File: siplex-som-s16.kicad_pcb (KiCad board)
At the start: 6 copper layers, 30 x 30 mm, 47 parts, among them J1 RFShield_OnePiece, J2 Conn_01x20, J3 Conn_01x20, J4 Conn_01x20, J6 Conn_01x20, U1 STM32H743IIKx, U2 IS42S16160J-6BLI, U3 W25Q32JVZP, Y1 25MHz, Y2 32.768KHz

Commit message: Add power
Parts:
- added C34: 2u2, Capacitor_SMD:C_0402_1005Metric, F.Cu at (133.7, 106.0)
- added C35: 100n, Capacitor_SMD:C_0201_0603Metric, F.Cu at (132.7, 106.0)
- added C36: 1u, Capacitor_SMD:C_0402_1005Metric, F.Cu at (130.5, 109.4)
- added C37: 100n, Capacitor_SMD:C_0201_0603Metric, F.Cu at (130.5, 108.5)
- added C38: 1u, Capacitor_SMD:C_0402_1005Metric, F.Cu at (129.1, 92.1)
- added C39: 100n, Capacitor_SMD:C_0201_0603Metric, F.Cu at (129.1, 91.2)
- added L1: L_Small, Inductor_SMD:L_0402_1005Metric, F.Cu at (129.1, 93.2)
- added U4: AP2112K-3.3, Package_TO_SOT_SMD:SOT-23-5, F.Cu at (130.5, 106.0)
- moved C8 18.7 mm to (129.0, 89.3), turned to 90 degrees
- moved R2 18.0 mm to (133.6, 89.1), turned to -90 degrees
- moved C2 17.2 mm to (130.3, 88.8), turned to 90 degrees
- moved R3 11.6 mm to (142.1, 94.4), turned to 90 degrees
- moved C3 6.28 mm to (134.4, 89.1), turned to -90 degrees
- moved C1 5.60 mm to (129.1, 98.6)
- moved C10 4.27 mm to (132.8, 87.5), turned to -90 degrees
- moved C15 1.74 mm to (132.0, 87.5), turned to -90 degrees
- moved C6 1.67 mm to (139.7, 89.3), turned to 0 degrees
- moved R1 1.62 mm to (142.1, 91.4)
- moved C11 1.57 mm to (129.1, 97.3)
- moved C12 1.57 mm to (129.1, 95.6)
- moved C13 1.57 mm to (129.1, 96.4)
- moved C14 1.57 mm to (142.1, 92.9)
- moved C16 1.57 mm to (131.1, 89.0)
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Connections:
- C10 pad 2: +3V3 -> VDD_MCU
- C11 pad 2: +3V3 -> VDD_MCU
- C12 pad 2: +3V3 -> VDD_MCU
- C13 pad 2: +3V3 -> VDD_MCU
- C14 pad 2: +3V3 -> VDD_MCU
- C15 pad 2: +3V3 -> VDD_MCU
- C16 pad 2: +3V3 -> VDD_MCU
- C17 pad 2: +3V3 -> VDD_MCU
- C18 pad 2: +3V3 -> VDD_MCU
- C19 pad 2: +3V3 -> VDD_MCU
- C20 pad 2: +3V3 -> VDD_MCU
- C21 pad 2: +3V3 -> VDD_MCU
- C22 pad 2: +3V3 -> VDD_MCU
- C23 pad 2: +3V3 -> VDD_MCU
- C24 pad 2: +3V3 -> VDD_MCU
- C25 pad 2: +3V3 -> VDD_MCU
- C8 pad 1: +3V3 -> VDDA
- C9 pad 2: +3V3 -> VDDA
- R1 pad 1: +3V3 -> VDD_MCU
- R2 pad 1: +3V3 -> VDD_MCU
- U1 pad A3: unconnected-(U1-PE1-PadA3) -> /MCU/SDRAM_DQMH
- U1 pad A4: unconnected-(U1-PE0-PadA4) -> /MCU/SDRAM_DQML
- U1 pad B15: unconnected-(U1-PA12-PadB15) -> /MCU/USB_DP
- U1 pad B6: unconnected-(U1-PB6-PadB6) -> /MEMORY_FLASH/~{CS}
- U1 pad B7: unconnected-(U1-PG15-PadB7) -> /MCU/~{SDRAM_CAS}
- U1 pad C15: unconnected-(U1-PA11-PadC15) -> /MCU/USB_DN
- U1 pad C5: +3V3 -> VDD_MCU
- U1 pad C7: +3V3 -> VDD_MCU
- U1 pad C8: +3V3 -> VDD_MCU
- U1 pad C9: +3V3 -> VDD_MCU
- U1 pad E15: unconnected-(U1-PA9-PadE15) -> /MCU/USB_VBUS_DET
- U1 pad E2: unconnected-(U1-PF0-PadE2) -> /MCU/SDRAM_A0
- U1 pad F3: +3V3 -> VDD_MCU
- U1 pad F4: unconnected-(U1-PH2-PadF4) -> /MCU/SDRAM_CKE
- U1 pad G13: +3V3 -> VDD_MCU
- U1 pad G3: +3V3 -> VDD_MCU
- U1 pad H13: +3V3 -> VDD_MCU
- U1 pad H14: unconnected-(U1-PG8-PadH14) -> /MCU/SDRAM_CLK
- U1 pad H2: unconnected-(U1-PF2-PadH2) -> /MCU/SDRAM_A2
- U1 pad H3: unconnected-(U1-PF1-PadH3) -> /MCU/SDRAM_A1
- U1 pad J12: +3V3 -> VDD_MCU
- U1 pad J13: +3V3 -> VDD_MCU
- U1 pad J2: unconnected-(U1-PF3-PadJ2) -> /MCU/SDRAM_A3
- U1 pad J3: unconnected-(U1-PF4-PadJ3) -> /MCU/SDRAM_A4
- U1 pad J4: unconnected-(U1-PH5-PadJ4) -> /MCU/~{SDRAM_WE}
- U1 pad K1: unconnected-(U1-PF7-PadK1) -> /MEMORY_FLASH/IO2
- U1 pad K13: unconnected-(U1-PG5-PadK13) -> /MCU/SDRAM_BA1
- U1 pad K14: unconnected-(U1-PG4-PadK14) -> /MCU/SDRAM_BA0
- U1 pad K2: unconnected-(U1-PF6-PadK2) -> /MEMORY_FLASH/IO3
- U1 pad K3: unconnected-(U1-PF5-PadK3) -> /MCU/SDRAM_A5
- U1 pad K4: +3V3 -> VDD_MCU
- U1 pad L15: unconnected-(U1-PG2-PadL15) -> /MCU/SDRAM_A12
- U1 pad L2: unconnected-(U1-PF9-PadL2) -> /MEMORY_FLASH/DI(IO0)
- U1 pad L3: unconnected-(U1-PF8-PadL3) -> /MEMORY_FLASH/DO(IO1)
- U1 pad M4: unconnected-(U1-PC2_C-PadM4) -> /MCU/~{SDRAM_CS}
- U1 pad M6: unconnected-(U1-PB2-PadM6) -> /MEMORY_FLASH/CLK
- U1 pad M7: unconnected-(U1-PG1-PadM7) -> /MCU/SDRAM_A11
- U1 pad N10: +3V3 -> VDD_MCU
- U1 pad N6: unconnected-(U1-PF13-PadN6) -> /MCU/SDRAM_A7
- U1 pad N7: unconnected-(U1-PG0-PadN7) -> /MCU/SDRAM_A10
- U1 pad N8: +3V3 -> VDD_MCU
- U1 pad N9: +3V3 -> VDD_MCU
- U1 pad P1: +3V3 -> VDDA
- U1 pad P6: unconnected-(U1-PF12-PadP6) -> /MCU/SDRAM_A6
- U1 pad P7: unconnected-(U1-PF15-PadP7) -> /MCU/SDRAM_A9
- U1 pad R1: +3V3 -> VDDA
- U1 pad R6: unconnected-(U1-PF11-PadR6) -> /MCU/~{SDRAM_RAS}
- U1 pad R7: unconnected-(U1-PF14-PadR7) -> /MCU/SDRAM_A8
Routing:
- net GND: track 0.00 -> 21.9 mm, vias 0 -> 46
- net +3V3: track 24.7 -> 3.96 mm, vias 0 -> 7
- net VDD_MCU: track 0.00 -> 6.43 mm, vias 0 -> 14
- net Net-(U1-PC15): track 5.79 -> 0.46 mm, vias 0 -> 1
- net Net-(U1-PC14): track 5.09 -> 0.46 mm, vias 0 -> 1
- net Net-(U1-PH0): track 4.73 -> 0.46 mm, vias 0 -> 1
- net Net-(U1-PH1): track 3.17 -> 0.46 mm, vias 0 -> 1
- net /MCU/~{SDRAM_RAS}: track 0.00 -> 1.03 mm, vias 0 -> 2
- net /MCU/~{SDRAM_CAS}: track 0.00 -> 1.03 mm, vias 0 -> 2
- net /MCU/SDRAM_BA1: track 0.00 -> 1.03 mm, vias 0 -> 2
- net /MCU/SDRAM_BA0: track 0.00 -> 1.03 mm, vias 0 -> 2
- net /MCU/SDRAM_A8: track 0.00 -> 1.03 mm, vias 0 -> 2
- net /MCU/~{SDRAM_WE}: track 0.00 -> 1.03 mm, vias 0 -> 2
- net /MCU/SDRAM_A9: track 0.00 -> 1.03 mm, vias 0 -> 2
- net /MCU/SDRAM_A6: track 0.00 -> 1.03 mm, vias 0 -> 2
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- added copper zone on B.Cu, net GND
- added copper zone on F.Cu, net GND
- added copper zone on In1.Cu, net GND
- added copper zone on In4.Cu, net GND
- added copper zone on In2.Cu, net VDD_MCU

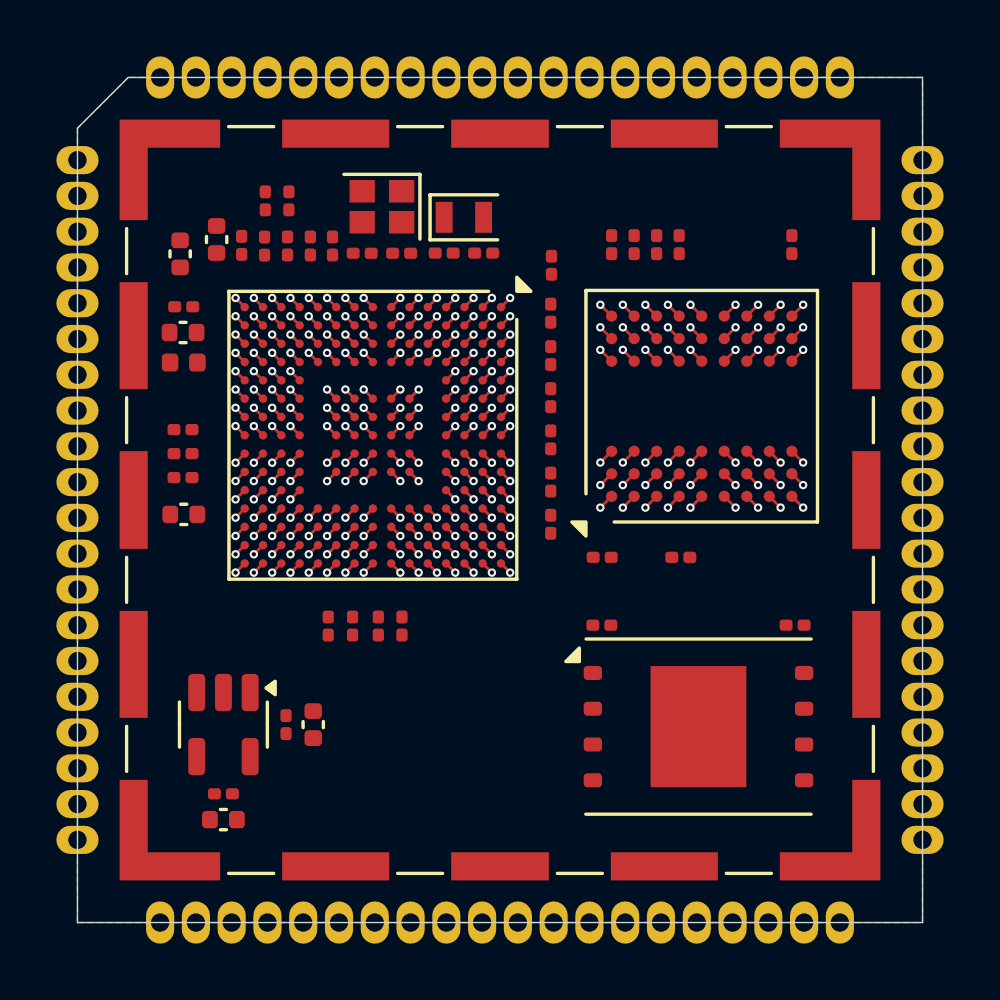
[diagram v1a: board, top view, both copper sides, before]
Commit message: Change to 8 layer, doing SDRAM traces
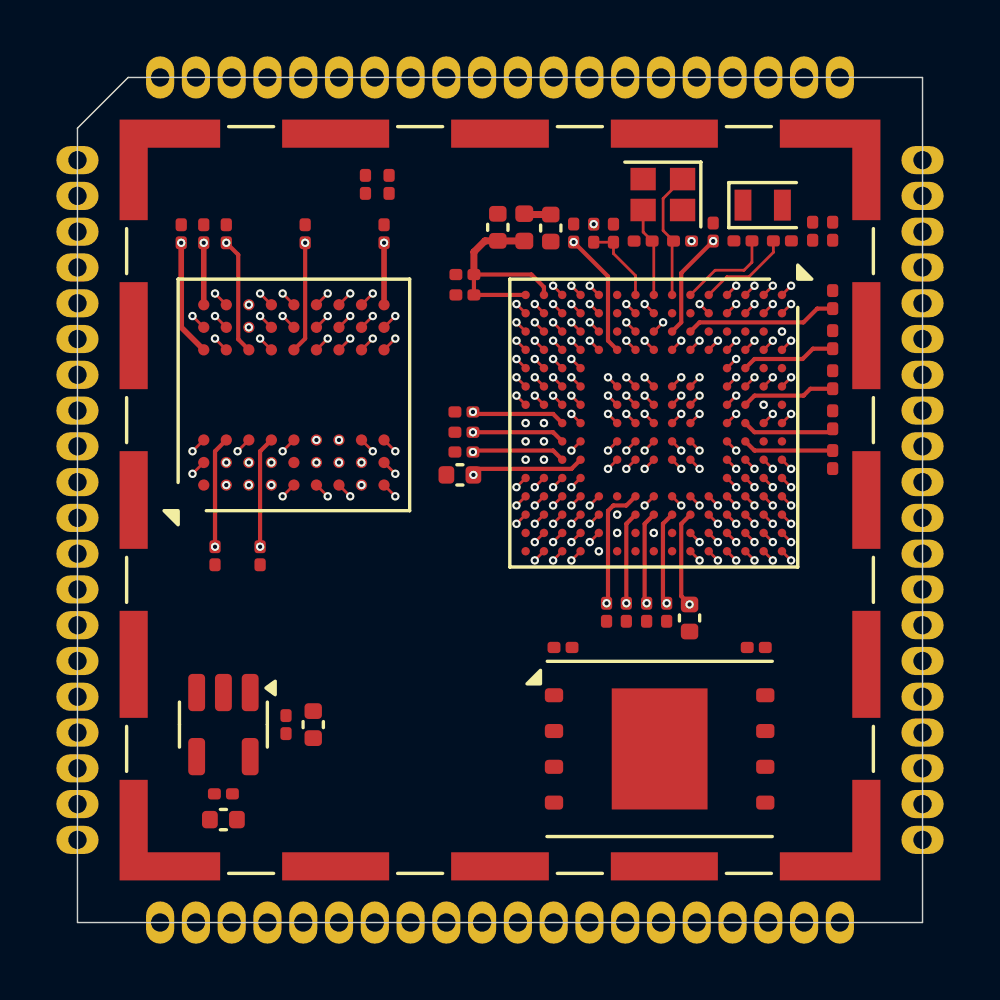
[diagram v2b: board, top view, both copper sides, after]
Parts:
- removed C38: 1u, Capacitor_SMD:C_0402_1005Metric
- added C40: 1u, Capacitor_SMD:C_0402_1005Metric, F.Cu at (142.1, 88.4)
- moved C2 21.5 mm to (147.0, 102.3), turned to -90 degrees
- moved C16 21.1 mm to (152.1, 91.0)
- moved C21 15.9 mm to (147.9, 88.6)
- moved C27 15.3 mm to (130.6, 88.6)
- moved C32 15.3 mm to (129.0, 88.6)
- moved C33 15.3 mm to (129.8, 88.6)
- moved C29 14.9 mm to (131.8, 100.1), turned to 90 degrees
- moved U2 14.5 mm to (133.0, 94.3)
- moved C28 14.5 mm to (136.2, 88.6)
- moved C26 13.7 mm to (130.2, 100.1), turned to 90 degrees
- moved C30 13.3 mm to (133.4, 88.6)
- moved L1 13.0 mm to (141.2, 88.4), turned to -90 degrees
- moved C8 11.3 mm to (140.2, 88.4)
- moved R3 11.0 mm to (151.4, 88.5), turned to -90 degrees
- moved C6 10.6 mm to (150.3, 88.9)
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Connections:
- U1 pad B12: unconnected-(U1-PD0-PadB12) -> /MCU/SDRAM_DQ2
- U1 pad C12: unconnected-(U1-PD1-PadC12) -> /MCU/SDRAM_DQ3
- U1 pad L14: unconnected-(U1-PD15-PadL14) -> /MCU/SDRAM_DQ1
- U1 pad M14: unconnected-(U1-PD14-PadM14) -> /MCU/SDRAM_DQ0
- U1 pad N11: unconnected-(U1-PE13-PadN11) -> /MCU/SDRAM_DQ10
- U1 pad N15: unconnected-(U1-PD10-PadN15) -> /MCU/SDRAM_DQ15
- U1 pad P10: unconnected-(U1-PE11-PadP10) -> /MCU/SDRAM_DQ8
- U1 pad P11: unconnected-(U1-PE14-PadP11) -> /MCU/SDRAM_DQ11
- U1 pad P14: unconnected-(U1-PD9-PadP14) -> /MCU/SDRAM_DQ14
- U1 pad P15: unconnected-(U1-PD8-PadP15) -> /MCU/SDRAM_DQ13
- U1 pad P8: unconnected-(U1-PE8-PadP8) -> /MCU/SDRAM_DQ5
- U1 pad P9: unconnected-(U1-PE9-PadP9) -> /MCU/SDRAM_DQ6
- U1 pad R10: unconnected-(U1-PE12-PadR10) -> /MCU/SDRAM_DQ9
- U1 pad R11: unconnected-(U1-PE15-PadR11) -> /MCU/SDRAM_DQ12
- U1 pad R8: unconnected-(U1-PE7-PadR8) -> /MCU/SDRAM_DQ4
- U1 pad R9: unconnected-(U1-PE10-PadR9) -> /MCU/SDRAM_DQ7
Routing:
- net VDD_MCU: track 6.43 -> 52.3 mm, vias 14 -> 10
- net /MCU/SDRAM_DQMH: track 1.03 -> 28.4 mm
- net +3V3: track 3.96 -> 24.5 mm
- net /MCU/SDRAM_DQ15: track 0.57 -> 16.2 mm, vias 1 -> 2
- net /MCU/SDRAM_CLK: track 1.03 -> 15.5 mm
- net /MCU/SDRAM_A0: track 1.03 -> 15.5 mm
- net /MCU/SDRAM_DQ13: track 0.57 -> 13.9 mm, vias 1 -> 2
- net /MCU/SDRAM_DQ11: track 0.57 -> 13.9 mm, vias 1 -> 2
- net /MCU/SDRAM_A12: track 1.03 -> 14.1 mm
- net /MCU/SDRAM_A1: track 1.03 -> 13.2 mm
- net /MCU/SDRAM_DQ14: track 0.57 -> 12.7 mm, vias 1 -> 2
- net /MCU/SDRAM_DQ10: track 0.57 -> 12.5 mm, vias 1 -> 2
- net /MCU/SDRAM_A11: track 1.03 -> 12.8 mm
- net /MCU/SDRAM_DQ12: track 0.57 -> 11.7 mm, vias 1 -> 2
- net /MCU/SDRAM_DQ8: track 0.57 -> 11.4 mm, vias 1 -> 2
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- removed copper zone on B.Cu, net GND
- removed copper zone on F.Cu, net GND
- removed copper zone on In1.Cu, net GND
- removed copper zone on In4.Cu, net GND
- removed copper zone on In2.Cu, net VDD_MCU
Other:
- copper layers 6 -> 8

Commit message: Finished SDRAM, QSPI FLASH (trace length not matched yet)
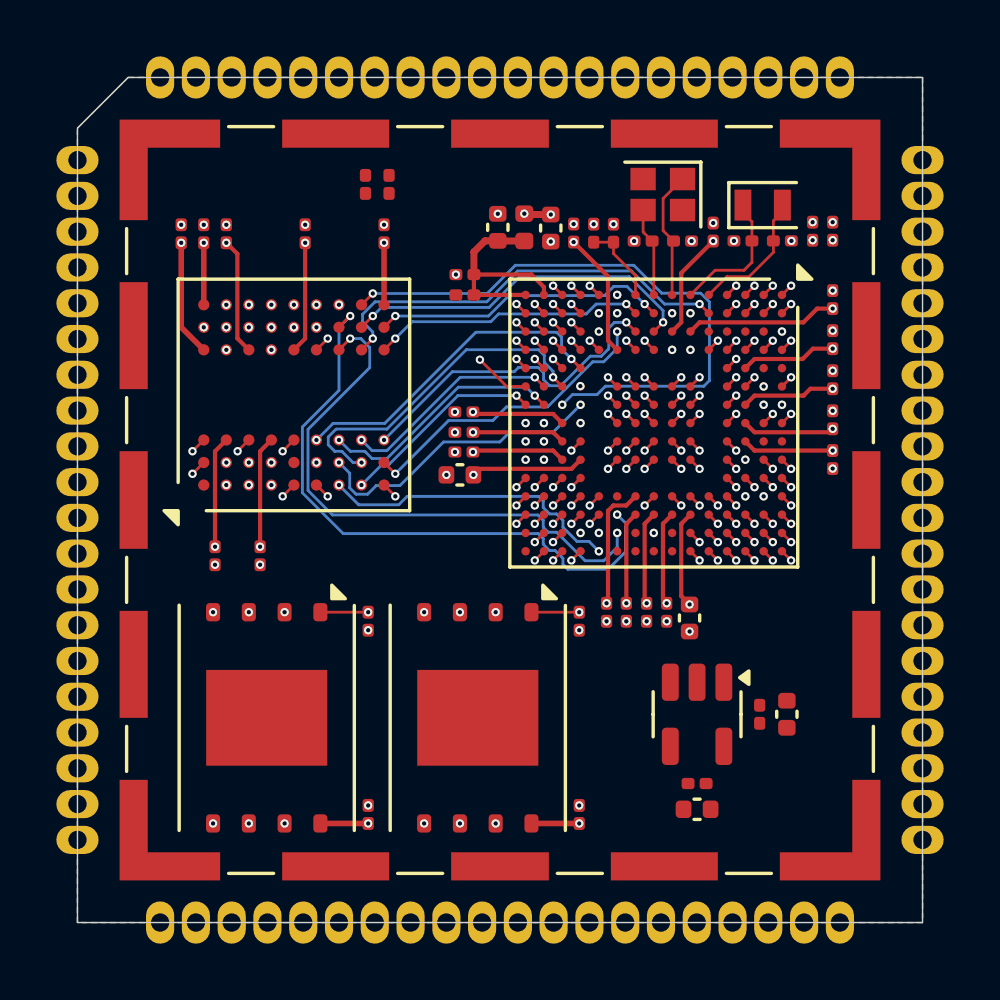
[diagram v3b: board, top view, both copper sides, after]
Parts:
- added C38: 100n, Capacitor_SMD:C_0201_0603Metric, F.Cu at (143.1, 109.2)
- added R5: 10K, Resistor_SMD:R_0201_0603Metric, F.Cu at (143.1, 102.4)
- added U5: W25Q32JVZP, Package_SON:WSON-8-1EP_8x6mm_P1.27mm_EP3.4x4.3mm, F.Cu at (139.5, 105.8)
- moved C34 16.8 mm to (150.5, 105.7)
- moved C35 16.8 mm to (149.5, 105.7)
- moved C36 16.8 mm to (147.3, 109.1)
- moved C37 16.8 mm to (147.3, 108.1)
- moved U4 16.8 mm to (147.3, 105.7)
- moved C31 15.0 mm to (135.6, 109.2), turned to 90 degrees
- moved U3 14.0 mm to (132.0, 105.8), turned to -90 degrees
- moved R4 6.98 mm to (135.6, 102.4), turned to 90 degrees
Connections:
- net /MEMORY_FLASH/CLK renamed /MCU/FLASH_CLK
- net /MEMORY_FLASH/IO2 renamed /MCU/FLASH_BK1_IO2
- net /MEMORY_FLASH/IO3 renamed /MCU/FLASH_BK1_IO3
- net /MEMORY_FLASH/~{CS} renamed /MCU/~{FLASH_BK1_CS}
- C10 pad 2: VDD_MCU -> +3V3
- C11 pad 2: VDD_MCU -> +3V3
- C12 pad 2: VDD_MCU -> +3V3
- C13 pad 2: VDD_MCU -> +3V3
- C14 pad 2: VDD_MCU -> +3V3
- C15 pad 2: VDD_MCU -> +3V3
- C16 pad 2: VDD_MCU -> +3V3
- C17 pad 2: VDD_MCU -> +3V3
- C18 pad 2: VDD_MCU -> +3V3
- C19 pad 2: VDD_MCU -> +3V3
- C20 pad 2: VDD_MCU -> +3V3
- C21 pad 2: VDD_MCU -> +3V3
- C22 pad 2: VDD_MCU -> +3V3
- C23 pad 2: VDD_MCU -> +3V3
- C24 pad 2: VDD_MCU -> +3V3
- C25 pad 2: VDD_MCU -> +3V3
- C36 pad 1: VDD_MCU -> +3V3
- C37 pad 1: VDD_MCU -> +3V3
- C40 pad 1: VDD_MCU -> +3V3
- L1 pad 1: VDD_MCU -> +3V3
- R1 pad 1: VDD_MCU -> +3V3
- R2 pad 1: VDD_MCU -> +3V3
- U1 pad A7: unconnected-(U1-PG14-PadA7) -> /MCU/FLASH_BK2_IO3
- U1 pad B13: unconnected-(U1-PC11-PadB13) -> /MCU/~{FLASH_BK2_CS}
- U1 pad C10: unconnected-(U1-PG9-PadC10) -> /MCU/FLASH_BK2_IO2
- U1 pad C5: VDD_MCU -> +3V3
- U1 pad C7: VDD_MCU -> +3V3
- U1 pad C8: VDD_MCU -> +3V3
- U1 pad C9: VDD_MCU -> +3V3
- U1 pad F3: VDD_MCU -> +3V3
- U1 pad F4: /MCU/SDRAM_CKE -> /MCU/FLASH_BK2_IO0
- U1 pad G13: VDD_MCU -> +3V3
- U1 pad G3: VDD_MCU -> +3V3
- U1 pad G4: unconnected-(U1-PH3-PadG4) -> /MCU/FLASH_BK2_IO1
- U1 pad H13: VDD_MCU -> +3V3
- U1 pad J12: VDD_MCU -> +3V3
- U1 pad J13: VDD_MCU -> +3V3
- U1 pad K4: VDD_MCU -> +3V3
- U1 pad L2: /MEMORY_FLASH/DI(IO0) -> /MCU/FLASH_BK1_IO1
- U1 pad L3: /MEMORY_FLASH/DO(IO1) -> /MCU/FLASH_BK1_IO0
- U1 pad M5: unconnected-(U1-PC3_C-PadM5) -> /MCU/SDRAM_CKE
- U1 pad N10: VDD_MCU -> +3V3
- U1 pad N8: VDD_MCU -> +3V3
- U1 pad N9: VDD_MCU -> +3V3
- U3 pad 2: /MEMORY_FLASH/DO(IO1) -> /MCU/FLASH_BK1_IO1
- U3 pad 5: /MEMORY_FLASH/DI(IO0) -> /MCU/FLASH_BK1_IO0
- U4 pad 5: VDD_MCU -> +3V3
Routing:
- net +3V3: track 24.5 -> 80.2 mm, vias 7 -> 29
- net VDD_MCU: track 52.3 -> 0.00 mm, vias 10 -> 0
- net /MCU/FLASH_CLK: track 0.46 -> 30.5 mm, vias 1 -> 3
- net /MCU/SDRAM_DQML: track 1.03 -> 27.3 mm
- net /MCU/FLASH_BK1_IO0: track 0.00 -> 26.2 mm, vias 0 -> 2
- net /MCU/FLASH_BK1_IO3: track 0.00 -> 26.2 mm, vias 0 -> 2
- net /MCU/FLASH_BK2_IO0: track 0.00 -> 24.4 mm, vias 0 -> 2
- net /MCU/SDRAM_DQ3: track 0.48 -> 24.2 mm
- net /MCU/SDRAM_DQ2: track 1.03 -> 24.2 mm
- net /MCU/~{FLASH_BK1_CS}: track 0.46 -> 23.3 mm, vias 1 -> 2
- net /MCU/SDRAM_BA1: track 0.57 -> 22.1 mm
- net /MCU/SDRAM_DQ6: track 0.57 -> 21.8 mm
- net /MCU/FLASH_BK1_IO2: track 0.00 -> 21.1 mm, vias 0 -> 2
- net /MCU/SDRAM_A10: track 1.03 -> 21.8 mm
- net /MCU/FLASH_BK2_IO3: track 0.00 -> 20.8 mm, vias 0 -> 2
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- added copper zone on In4.Cu, net +3V3
- added copper zone on B.Cu, net GND
- added copper zone on F.Cu, net GND
- added copper zone on In1.Cu, net GND
- added copper zone on In4.Cu, net GND
- added copper zone on In6.Cu, net GND

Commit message: Change to via-in-pad mode
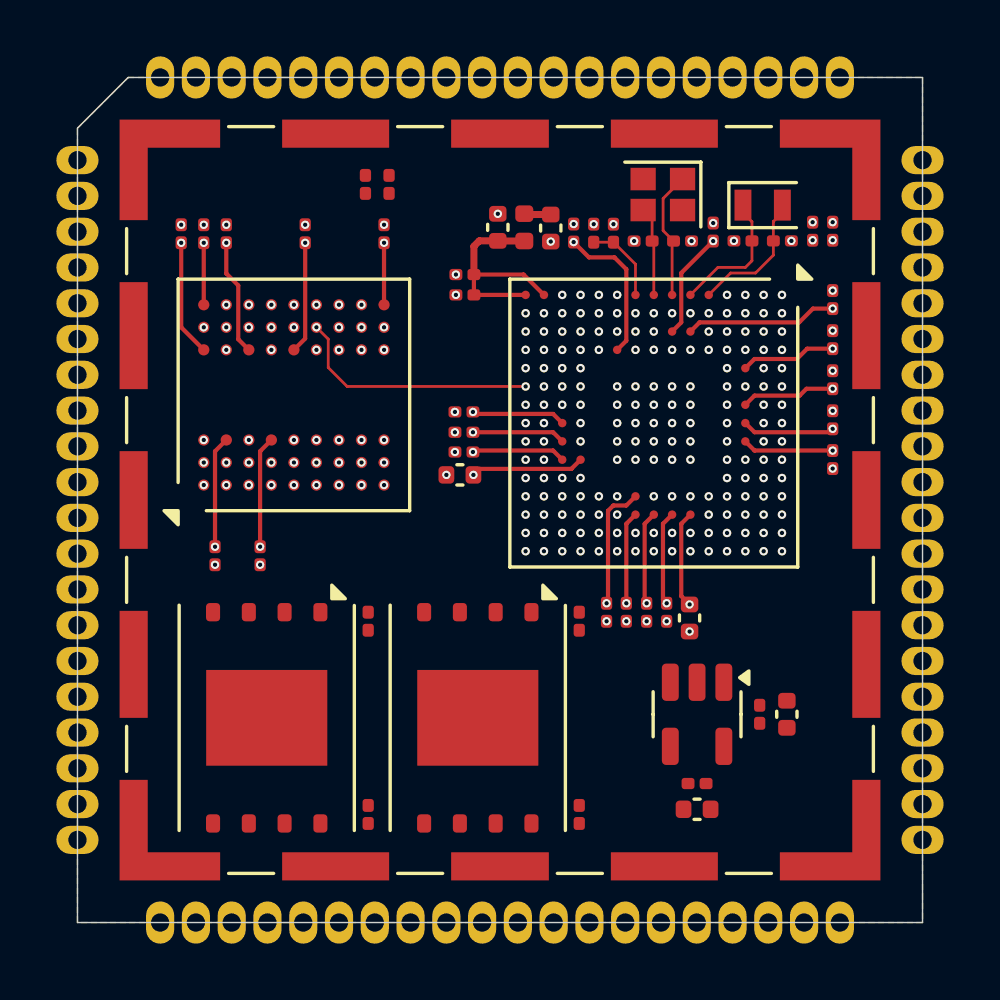
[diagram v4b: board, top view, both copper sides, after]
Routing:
- net /MCU/FLASH_CLK: track 30.5 -> 0.00 mm, vias 3 -> 1
- net /MCU/FLASH_BK1_IO0: track 26.2 -> 0.00 mm, vias 2 -> 1
- net /MCU/FLASH_BK1_IO3: track 26.2 -> 0.00 mm, vias 2 -> 1
- net /MCU/FLASH_BK2_IO0: track 24.4 -> 0.00 mm, vias 2 -> 1
- net /MCU/~{FLASH_BK1_CS}: track 23.3 -> 0.00 mm, vias 2 -> 1
- net /MCU/SDRAM_BA1: track 22.1 -> 0.00 mm
- net /MCU/SDRAM_A10: track 21.8 -> 0.00 mm
- net /MCU/FLASH_BK1_IO2: track 21.1 -> 0.00 mm, vias 2 -> 1
- net /MCU/FLASH_BK2_IO3: track 20.8 -> 0.00 mm, vias 2 -> 1
- net /MCU/SDRAM_BA0: track 20.2 -> 0.00 mm
- net GND: track 19.4 -> 0.00 mm, vias 81 -> 79
- net /MCU/FLASH_BK1_IO1: track 18.9 -> 0.00 mm, vias 2 -> 1
- net /MCU/SDRAM_A0: track 15.1 -> 0.00 mm
- net /MCU/SDRAM_DQ9: track 11.3 -> 25.6 mm
- net /MCU/FLASH_BK2_IO1: track 14.1 -> 0.00 mm, vias 2 -> 1
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
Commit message: Finished SDRAM_DATA
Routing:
- net /MCU/SDRAM_A2: track 0.00 -> 23.8 mm
- net /MCU/SDRAM_A3: track 0.00 -> 23.6 mm
- net /MCU/SDRAM_A10: track 0.00 -> 21.9 mm
- net /MCU/SDRAM_A0: track 0.00 -> 21.1 mm
- net /MCU/SDRAM_DQ8: track 10.0 -> 25.7 mm
- net /MCU/SDRAM_DQ12: track 11.4 -> 26.0 mm
- net /MCU/SDRAM_DQ10: track 12.0 -> 26.0 mm
- net /MCU/SDRAM_DQ14: track 12.3 -> 26.0 mm
- net /MCU/SDRAM_A1: track 0.00 -> 13.0 mm
- net /MCU/SDRAM_A11: track 0.00 -> 12.3 mm
- net /MCU/SDRAM_DQ13: track 13.5 -> 25.8 mm
- net /MCU/SDRAM_A9: track 0.00 -> 11.7 mm
- net /MCU/SDRAM_DQ11: track 14.1 -> 25.7 mm
- net /MCU/SDRAM_A7: track 0.00 -> 11.0 mm
- net /MCU/SDRAM_A4: track 0.00 -> 10.9 mm
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
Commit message: Finished SDRAM_ADDRESS
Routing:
- net /MCU/SDRAM_A8: track 8.77 -> 22.8 mm
- net /MCU/SDRAM_A6: track 9.22 -> 22.8 mm
- net /MCU/SDRAM_A12: track 10.6 -> 22.8 mm
- net /MCU/SDRAM_A5: track 10.9 -> 22.9 mm
- net /MCU/SDRAM_A4: track 10.9 -> 22.8 mm
- net /MCU/SDRAM_A7: track 11.0 -> 22.8 mm
- net /MCU/SDRAM_A9: track 11.7 -> 22.8 mm
- net /MCU/SDRAM_A11: track 12.3 -> 22.9 mm
- net /MCU/SDRAM_A1: track 13.0 -> 22.8 mm
- net /MCU/SDRAM_A0: track 21.1 -> 22.9 mm
- net /MCU/SDRAM_A10: track 21.9 -> 22.9 mm
- net /MCU/SDRAM_A2: track 23.8 -> 22.8 mm
- net /MCU/SDRAM_A3: track 23.6 -> 22.8 mm
